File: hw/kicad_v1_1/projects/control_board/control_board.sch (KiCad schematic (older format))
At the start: 7 parts, among them CON1 161-0725-E, P1 CONN_02X12_isolate_hv, P4 CONN_01X01, P5 CONN_01X01, P6 CONN_01X01, P7 CONN_01X01

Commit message: Schematic Work Complete
Check in schematic work before touching PCB. This should give me a point
to go back to if it all goes to hell.
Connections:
- net labels added: +180V, +5V, SEL_COL, SEL_N0_A, SEL_N0_B, SEL_N0_C, SEL_N0_D, SEL_N1_A, SEL_N1_B, SEL_N1_C, SEL_N1_D, SEL_N2_A, SEL_N2_B, SEL_N2_C, SEL_N2_D, SEL_N3_A, SEL_N3_B, SEL_N3_C, SEL_N3_D
- net labels removed: +170V, +3V3, SEL_DOT_BOT, SEL_DOT_TOP, SEL_EIGHT, SEL_FIVE, SEL_FOUR, SEL_NINE, SEL_NIX0, SEL_NIX1, SEL_NIX2, SEL_NIX3, SEL_ONE, SEL_SEVEN, SEL_SIX, SEL_THREE, SEL_TWO, SEL_ZERO
- no-connect marks 6 -> 5

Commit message: Complete with errors
Check in before moving header. Currently the headers don't match up. If
I'm going to connect them with standard header I need to move it
significantly. Check in as a roll back point.
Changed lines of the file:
@@
 F0 "Nixie Power Supply" 50
 F1 "nixie_power_supply.sch" 50
-F2 "180V_EN" I L 5100 4100 60
+F2 "180V_SHDN" I L 5100 4100 60
 $EndSheet
 $Sheet
@@
 	7400 3000 7950 3000
 Wire Wire Line
-	7400 3100 7950 3100
+	6350 3100 6900 3100
 Text Label 4050 2050 0    60   ~ 0
 SEL_N0_A
@@
 F17 "SEL_N2_D" O R 3800 3150 60
 F18 "COL_SEL" O R 3800 3650 60
-F19 "180V_EN" O R 3800 4100 60
+F19 "180V_SHDN" O R 3800 4100 60
 $EndSheet
 Wire Wire Line
@@
 	6350 3000 6900 3000
 Wire Wire Line
-	6900 3100 5950 3100
-Wire Wire Line
-	5950 3100 5950 2850
+	8350 3100 7400 3100
+Wire Wire Line
+	8350 3100 8350 2850
 $Comp
 L +5V #PWR06
 U 1 1 581FD7A7
-P 5950 2850
-F 0 "#PWR06" H 5950 2700 50  0001 C CNN
-F 1 "+5V" H 5950 2990 50  0000 C CNN
-F 2 "" H 5950 2850 50  0000 C CNN
-F 3 "" H 5950 2850 50  0000 C CNN
-	1    5950 2850
+P 8350 2850
+F 0 "#PWR06" H 8350 2700 50  0001 C CNN
+F 1 "+5V" H 8350 2990 50  0000 C CNN
+F 2 "" H 8350 2850 50  0000 C CNN
+F 3 "" H 8350 2850 50  0000 C CNN
+	1    8350 2850
 	1    0    0    -1
 $EndComp
@@
 Text Label 4050 3650 0    60   ~ 0
 SEL_COL
-Text Label 7500 3100 0    60   ~ 0
+Text Label 6400 3100 0    60   ~ 0
 SEL_COL
+Text Label 7500 2700 0    60   ~ 0
+SEL_N0_A
+Text Label 7500 2800 0    60   ~ 0
+SEL_N0_B
+Text Label 7500 2900 0    60   ~ 0
+SEL_N0_C
+Text Label 7500 3000 0    60   ~ 0
+SEL_N0_D
 Text Label 6400 2700 0    60   ~ 0
-SEL_N0_A
+SEL_N1_A
 Text Label 6400 2800 0    60   ~ 0
-SEL_N0_B
+SEL_N1_B
 Text Label 6400 2900 0    60   ~ 0
-SEL_N0_C
+SEL_N1_C
 Text Label 6400 3000 0    60   ~ 0
-SEL_N0_D
-Text Label 7500 2700 0    60   ~ 0
-SEL_N1_A
-Text Label 7500 2800 0    60   ~ 0
-SEL_N1_B
-Text Label 7500 2900 0    60   ~ 0
-SEL_N1_C
-Text Label 7500 3000 0    60   ~ 0
 SEL_N1_D
+Text Label 7500 2300 0    60   ~ 0
+SEL_N3_A
+Text Label 7500 2400 0    60   ~ 0
+SEL_N3_B
+Text Label 7500 2500 0    60   ~ 0
+SEL_N3_C
+Text Label 7500 2600 0    60   ~ 0
+SEL_N3_D
 Text Label 6400 2300 0    60   ~ 0
-SEL_N3_A
+SEL_N2_A
 Text Label 6400 2400 0    60   ~ 0
-SEL_N3_B
+SEL_N2_B
+Text Label 6400 2600 0    60   ~ 0
+SEL_N2_D
 Text Label 6400 2500 0    60   ~ 0
-SEL_N3_C
-Text Label 6400 2600 0    60   ~ 0
-SEL_N3_D
-Text Label 7500 2300 0    60   ~ 0
-SEL_N2_A
-Text Label 7500 2400 0    60   ~ 0
-SEL_N2_B
-Text Label 7500 2600 0    60   ~ 0
-SEL_N2_D
-Text Label 7500 2500 0    60   ~ 0
 SEL_N2_C
 $Comp

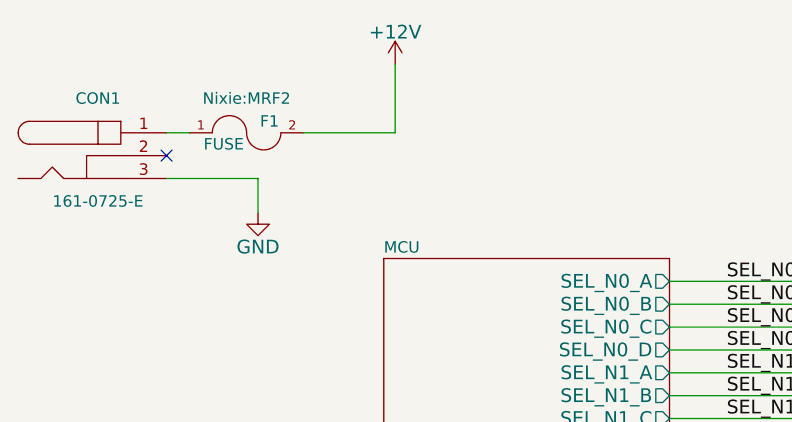
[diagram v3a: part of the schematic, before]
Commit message: Final Release
Update with trimming and bug fixes. This is what is being delivered as a
V1.1.0 release.
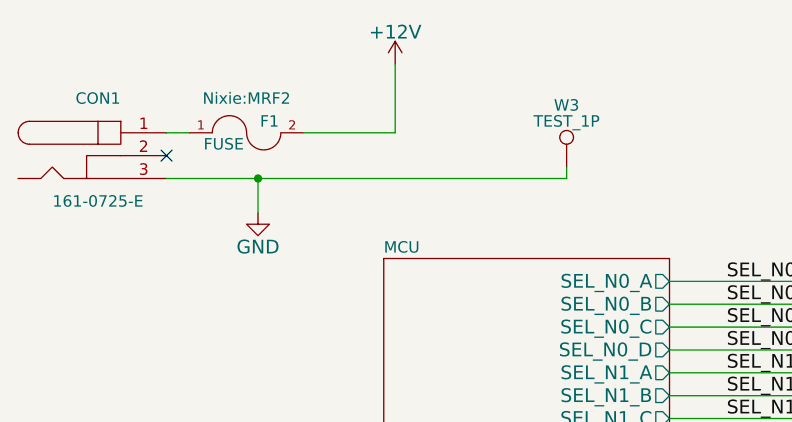
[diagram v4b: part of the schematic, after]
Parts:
- added W3: TEST_1P, Measurement_Points:Test_Point_Keystone_5019_Minature, symbol TEST_1P
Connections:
- wire segments 57 -> 58
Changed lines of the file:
@@
 Sheet 1 6
 Title "Control Board"
-Date "2016-09-14"
-Rev "1.0"
+Date "2016-11-21"
+Rev "1.1"
 Comp ""
 Comment1 ""
@@
 	2600 1400 2600 1100
 Wire Wire Line
-	1600 1600 2000 1600
+	1600 1600 3350 1600
 Wire Wire Line
 	2000 1600 2000 1750
@@
 	1    0    0    -1
 $EndComp
+Connection ~ 2000 1600
+$Comp
+L TEST_1P W3
+U 1 1 583539C0
+P 3350 1550
+F 0 "W3" H 3350 1820 50  0000 C CNN
+F 1 "TEST_1P" H 3350 1750 50  0000 C CNN
+F 2 "Measurement_Points:Test_Point_Keystone_5019_Minature" H 3550 1550 50  0001 C CNN
+F 3 "" H 3550 1550 50  0000 C CNN
+	1    3350 1550
+	1    0    0    -1
+$EndComp
+Wire Wire Line
+	3350 1600 3350 1550
 $EndSCHEMATC
